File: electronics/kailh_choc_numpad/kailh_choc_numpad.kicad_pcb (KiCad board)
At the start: 2 copper layers, 100 x 88 mm, 135 parts, among them J1 Conn_01x06, U1 PCA9554, U2 PCA9535

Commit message: silk placement completed
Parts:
- moved N1 71.3 mm to (143.2, 84.4)
- moved C2 0.07 mm to (140.0, 126.1)
- moved D34 0.05 mm to (219.0, 145.4)
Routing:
- net VSS: track 50.4 -> 51.0 mm

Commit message: updated broken IC footprint, added OHW logo
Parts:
- added N2: OHWLOGO, Symbol:OSHW-Symbol_8.9x8mm_SilkScreen, B.Cu at (142.4, 79.5)

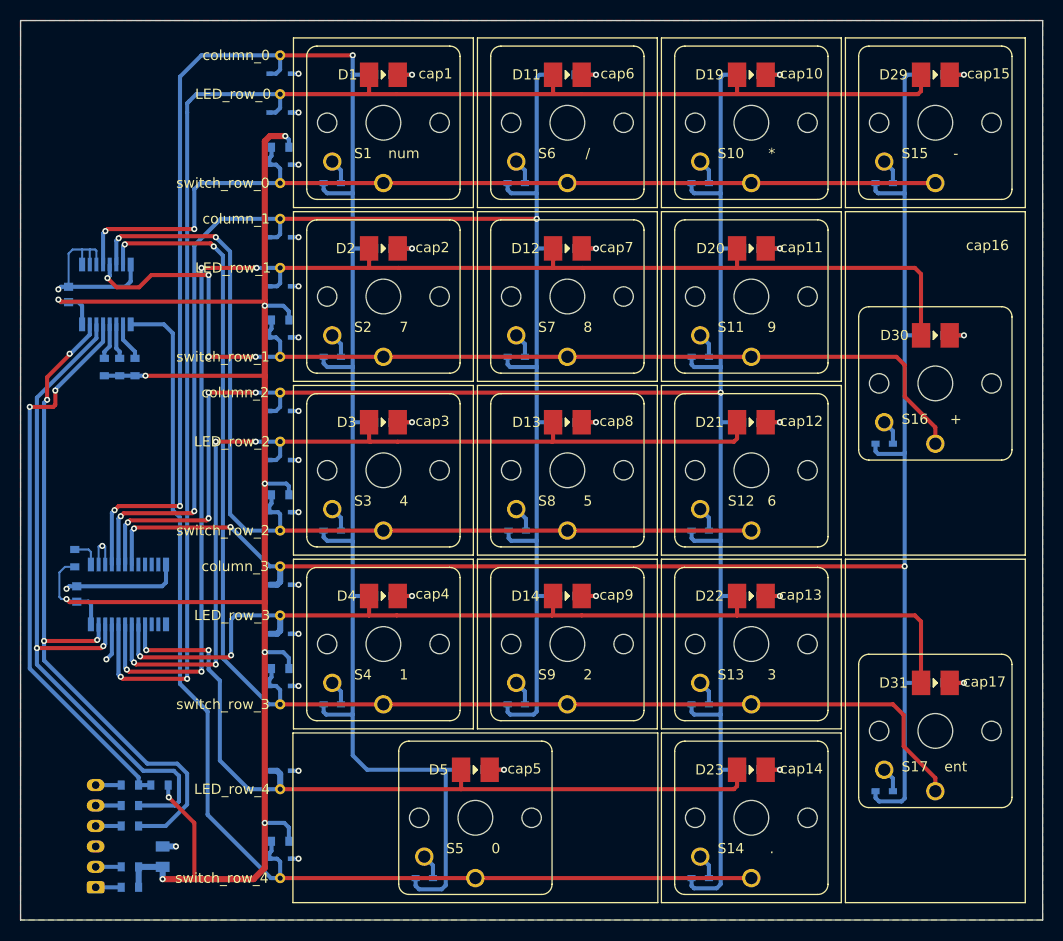
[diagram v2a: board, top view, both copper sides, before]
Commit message: added mounting holes
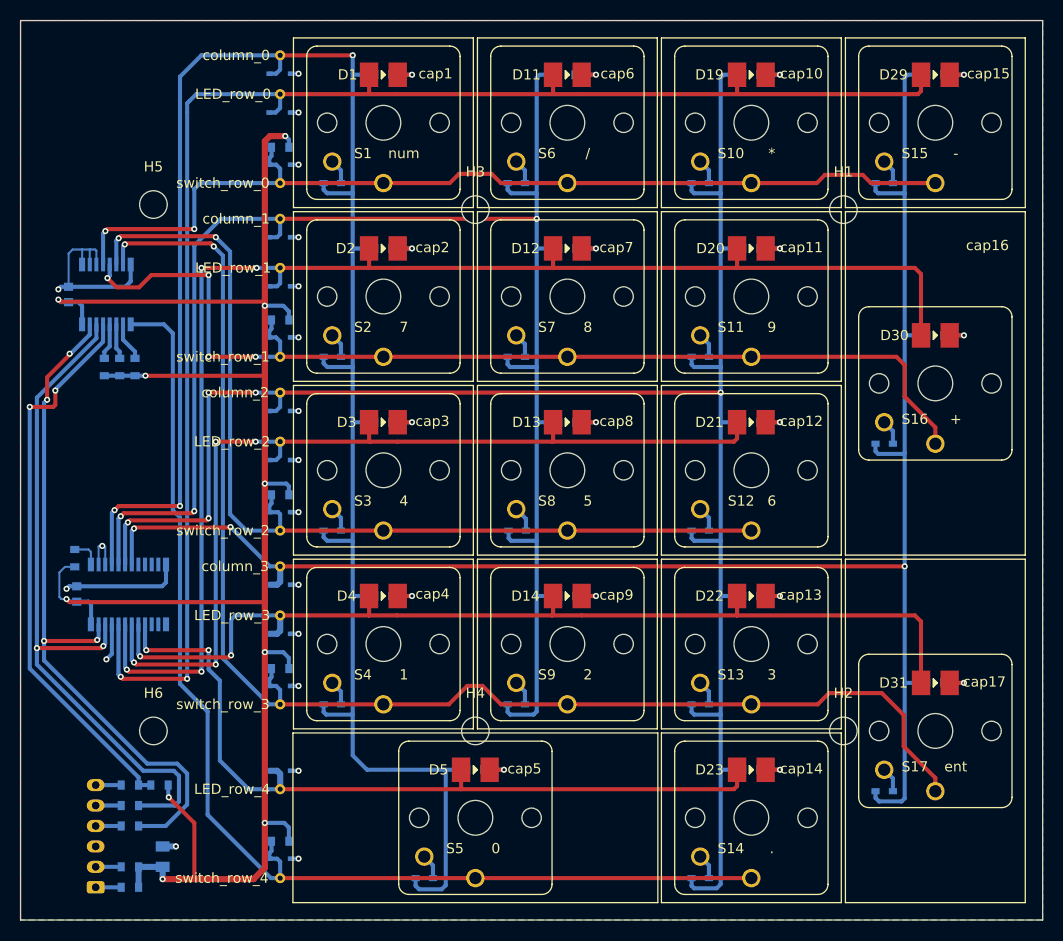
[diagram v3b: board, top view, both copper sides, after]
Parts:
- added H1: M2.5, MountingHole:MountingHole_2.7mm_M2.5, F.Cu at (215.0, 88.5)
- added H2: M2.5, MountingHole:MountingHole_2.7mm_M2.5, F.Cu at (215.0, 139.5)
- added H3: M2.5, MountingHole:MountingHole_2.7mm_M2.5, F.Cu at (179.0, 88.5)
- added H4: M2.5, MountingHole:MountingHole_2.7mm_M2.5, F.Cu at (179.0, 139.5)
- added H5: M2.5, MountingHole:MountingHole_2.7mm_M2.5, F.Cu at (147.5, 88.0)
- added H6: M2.5, MountingHole:MountingHole_2.7mm_M2.5, F.Cu at (147.5, 139.5)
- N1: value V20220626 -> V20220916
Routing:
- net /switch_row_3: track 133.6 -> 136.0 mm
- net /switch_row_0: track 93.2 -> 94.6 mm
